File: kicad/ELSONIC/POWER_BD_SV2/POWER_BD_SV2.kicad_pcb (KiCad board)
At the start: 2 copper layers, 150 x 98 mm, 97 parts, among them J2 SMW250-06P, J3 SMW250-02P, T1 EI2811BP, T2 EER28, U1 ICE3BR0665J, U2 H11AA1, U3 PC817, U4 ATTINY85-20PU_1, U5 MOC3021M, U6 LM7805_TO220

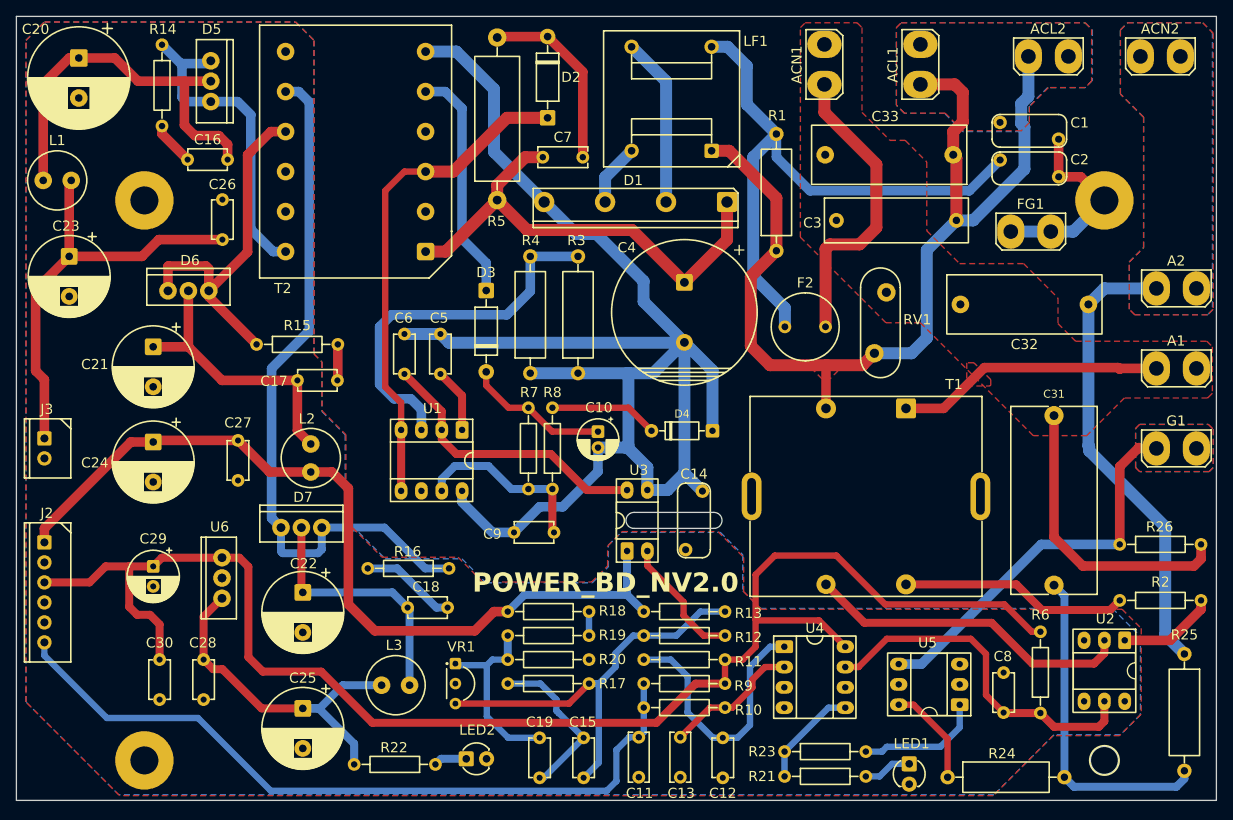
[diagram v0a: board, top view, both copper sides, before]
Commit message: 자동보정 구현: minDim/maxDim 기준 - setup()에서 ZC 주기 측정 후 minDim/maxDim 동적 계산 - maxDim = avgPeriod - 6 (margin) - minDim = avgPeriod * 62 / 166 - 2 - 50Hz/60Hz 및 오실레이터 편차 자동 대응
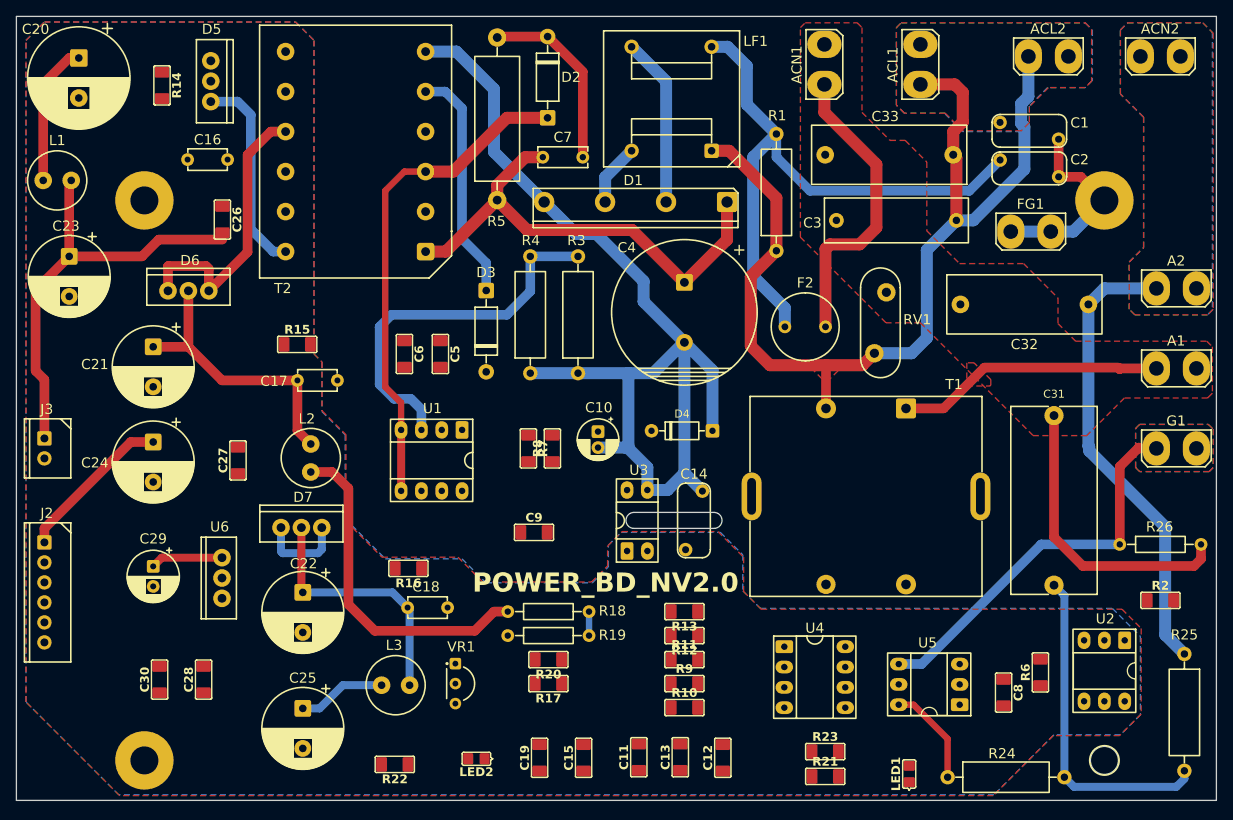
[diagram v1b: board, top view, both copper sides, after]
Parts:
- C11, C13: footprint 04_MyFoot_Passive:C_Disc_D6.0mm_P5.00mm -> 04_MyFoot_Passive:C_3216Metric
- C12, C26, C27, C28, C30, C5, C9: footprint 04_MyFoot_Passive:C_Disc_D4.7mm_T3.0mm_P5.00mm -> 04_MyFoot_Passive:C_3216Metric
- C15, C19, C6, C8: footprint 04_MyFoot_Passive:C_Disc_D4.7mm_P5.00mm -> 04_MyFoot_Passive:C_3216Metric
- LED1, LED2: footprint 03_MyFoot_Active:LED_D3.0mm -> 03_MyFoot_Active:LED_2012Metric
- R10, R11, R12, R13, R14, R15, R16, R17, R2, R20, R21, R22, R23, R6, R7, R8, R9: footprint 04_MyFoot_Passive:R_Axial_0.25W_P10.16mm -> 04_MyFoot_Passive:R_3216Metric
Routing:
- net +5V: track 187.4 -> 9.05 mm
- net /PWM_PW: track 95.0 -> 0.00 mm
- net Net-(T2-N1): track 88.3 -> 11.1 mm
- net Earth: track 192.9 -> 131.6 mm
- net Net-(C15-Pad1): track 53.2 -> 0.00 mm
- net +12V: track 107.8 -> 62.2 mm
- net /ZVC: track 44.2 -> 0.00 mm
- net Net-(T1-SA): track 41.0 -> 0.00 mm
- net Net-(U1-FB): track 35.9 -> 0.00 mm
- net +8V: track 45.4 -> 11.1 mm
- net Net-(U4-(PCINT5/RESET*/ADC0/dW)_PB5): track 33.2 -> 0.00 mm
- net Net-(D5-K): track 49.3 -> 17.8 mm
- net Net-(T1-SB): track 28.5 -> 0.00 mm
- net Net-(C19-Pad2): track 24.0 -> 0.00 mm
- net Net-(U1-VCC): track 22.7 -> 0.00 mm
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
